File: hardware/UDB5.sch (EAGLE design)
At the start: 106 parts, among them U1 DSPIC33FJ256GP710_, U10 MPU-6000QFN-24, U3 V_REG_LDOSMD, U5 V_REG_NCP50X, U6 D2523T_, U8 EEPROM-I2CSMD, U9 EM406, Y1 RESONATORSMD

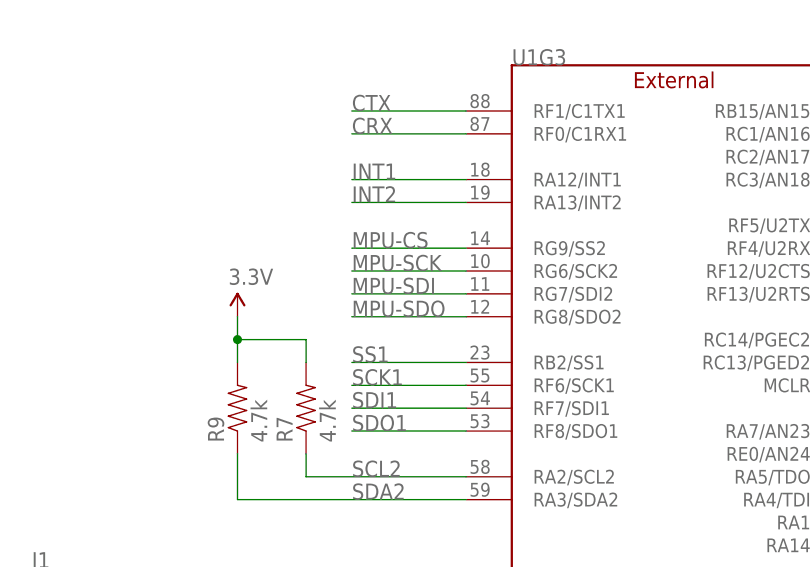
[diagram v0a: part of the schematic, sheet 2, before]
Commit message: v011
-swapped MPU MOSI and MISO, labeled them correctly.
-increased silk txt on PCB
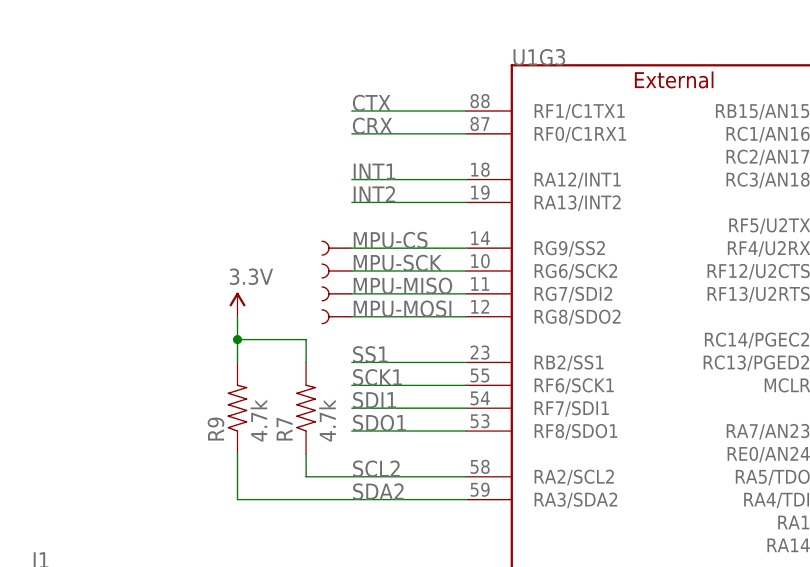
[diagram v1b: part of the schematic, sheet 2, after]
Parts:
- added TP1, TP2, TP3, TP4: TEST-POINT3, SparkFun-Passives:TEST-POINT3
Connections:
- removed net MPU-SDI: U10.SDA/SDI, U1G3.RG7/SDI2
- removed net MPU-SDO: U10.AD0/SDO, U1G3.RG8/SDO2
- new net MPU-MISO: TP3.1, U10.AD0/SDO, U1G3.RG7/SDI2
- new net MPU-MOSI: TP4.1, U10.SDA/SDI, U1G3.RG8/SDO2
- net MPU-CS: now also TP1.1
- net MPU-SCK: now also TP2.1
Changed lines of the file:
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@@
 <part name="LOGO1" library="SparkFun-Aesthetics" deviceset="LOGO-SFE" device="NW2"/>
 <part name="CC_TEXT1" library="SparkFun-Aesthetics" deviceset="CREATIVE_COMMONS" device=""/>
+<part name="TP1" library="SparkFun-Passives" deviceset="TEST-POINT" device="3"/>
+<part name="TP2" library="SparkFun-Passives" deviceset="TEST-POINT" device="3"/>
+<part name="TP3" library="SparkFun-Passives" deviceset="TEST-POINT" device="3"/>
+<part name="TP4" library="SparkFun-Passives" deviceset="TEST-POINT" device="3"/>
 </parts>
 <sheets>
@@
 </instance>
 <instance part="GND34" gate="1" x="22.86" y="7.62"/>
+<instance part="TP1" gate="G$1" x="154.94" y="149.86" smashed="yes" rot="R180"/>
+<instance part="TP2" gate="G$1" x="154.94" y="147.32" smashed="yes" rot="R180"/>
+<instance part="TP3" gate="G$1" x="154.94" y="144.78" smashed="yes" rot="R180"/>
+<instance part="TP4" gate="G$1" x="154.94" y="142.24" smashed="yes" rot="R180"/>
 </instances>
 <busses>
@@
 <label x="154.94" y="149.86" size="1.778" layer="95"/>
 <pinref part="U1" gate="G3" pin="RG9/SS2"/>
+<pinref part="TP1" gate="G$1" pin="1"/>
 </segment>
 </net>
@@
 <label x="154.94" y="147.32" size="1.778" layer="95"/>
 <pinref part="U1" gate="G3" pin="RG6/SCK2"/>
-</segment>
-</net>
-<net name="MPU-SDI" class="0">
+<pinref part="TP2" gate="G$1" pin="1"/>
+</segment>
+</net>
+<net name="MPU-MISO" class="0">
 <segment>
 <wire x1="167.64" y1="144.78" x2="154.94" y2="144.78" width="0.1524" layer="91"/>
 <label x="154.94" y="144.78" size="1.778" layer="95"/>
 <pinref part="U1" gate="G3" pin="RG7/SDI2"/>
-</segment>
-</net>
-<net name="MPU-SDO" class="0">
-<segment>
-<wire x1="167.64" y1="142.24" x2="154.94" y2="142.24" width="0.1524" layer="91"/>
-<label x="154.94" y="142.24" size="1.778" layer="95"/>
-<pinref part="U1" gate="G3" pin="RG8/SDO2"/>
+<pinref part="TP3" gate="G$1" pin="1"/>
 </segment>
 </net>
@@
 <label x="218.44" y="116.84" size="1.778" layer="95"/>
 <pinref part="U1" gate="G3" pin="RA14"/>
+</segment>
+</net>
+<net name="MPU-MOSI" class="0">
+<segment>
+<wire x1="167.64" y1="142.24" x2="154.94" y2="142.24" width="0.1524" layer="91"/>
+<label x="154.94" y="142.24" size="1.778" layer="95"/>
+<pinref part="U1" gate="G3" pin="RG8/SDO2"/>
+<pinref part="TP4" gate="G$1" pin="1"/>
 </segment>
 </net>
@@
 </segment>
 </net>
-<net name="MPU-SDO" class="0">
+<net name="MPU-MISO" class="0">
 <segment>
 <pinref part="U10" gate="G$1" pin="AD0/SDO"/>
 <wire x1="129.54" y1="50.8" x2="139.7" y2="50.8" width="0.1524" layer="91"/>
 <label x="132.08" y="50.8" size="1.778" layer="95"/>
-</segment>
-</net>
-<net name="MPU-SDI" class="0">
-<segment>
-<pinref part="U10" gate="G$1" pin="SDA/SDI"/>
-<wire x1="129.54" y1="48.26" x2="139.7" y2="48.26" width="0.1524" layer="91"/>
-<label x="132.08" y="48.26" size="1.778" layer="95"/>
 </segment>
 </net>
@@
 </segment>
 </net>
+<net name="MPU-MOSI" class="0">
+<segment>
+<pinref part="U10" gate="G$1" pin="SDA/SDI"/>
+<wire x1="129.54" y1="48.26" x2="139.7" y2="48.26" width="0.1524" layer="91"/>
+<label x="132.08" y="48.26" size="1.778" layer="95"/>
+</segment>
+</net>
